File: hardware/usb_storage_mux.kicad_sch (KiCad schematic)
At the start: 24 parts, among them J7 USB3_B, J8 USB3_B_Micro, J9 USB3_A, U6 TMUXHS4212

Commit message: WIP 1.1
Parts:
- removed J7: USB3_B, USB3Wurth:Wurth WR-COM USB 3.0 692221030100, symbol Connector:USB3_B
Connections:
- net HOST_DN renamed SHOST_DN
- net HOST_DP renamed SHOST_DP
- net HOST_SSRXN renamed SHOST_SSRXN
- net HOST_SSRXP renamed SHOST_SSRXP
- net HOST_SSTXN renamed SHOST_SSTXN
- net HOST_SSTXP renamed SHOST_SSTXP
- net _HOST_SSRXN renamed _SHOST_SSRXN
- net _HOST_SSRXP renamed _SHOST_SSRXP

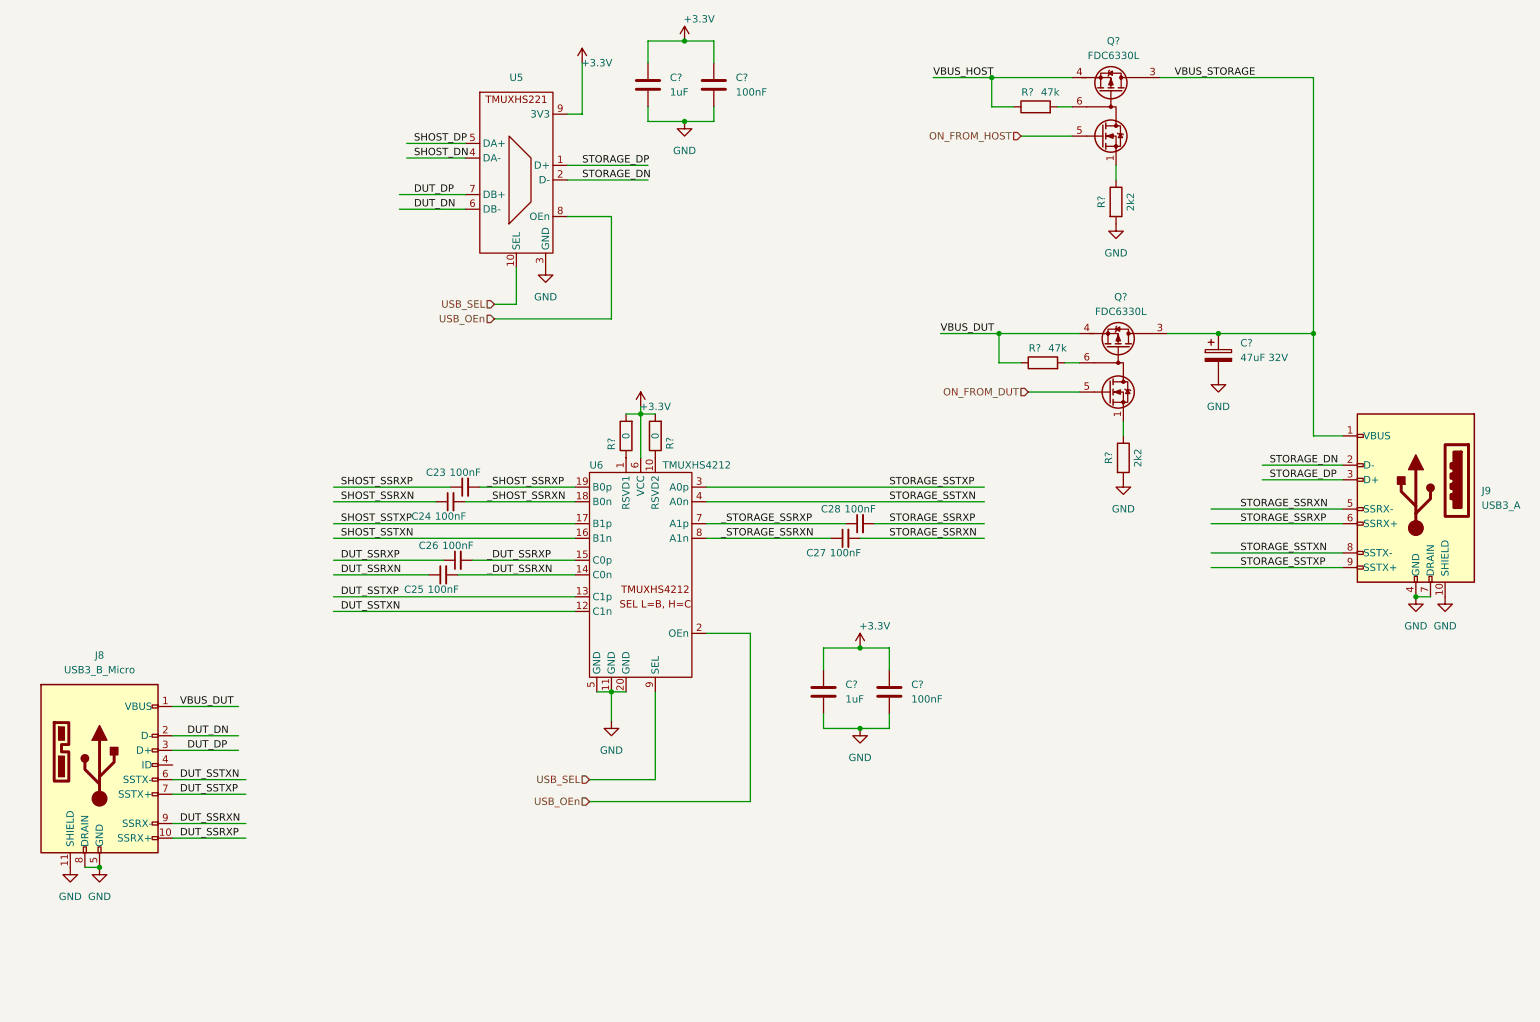
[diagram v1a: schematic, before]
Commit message: Started routing USB3 diff pairs
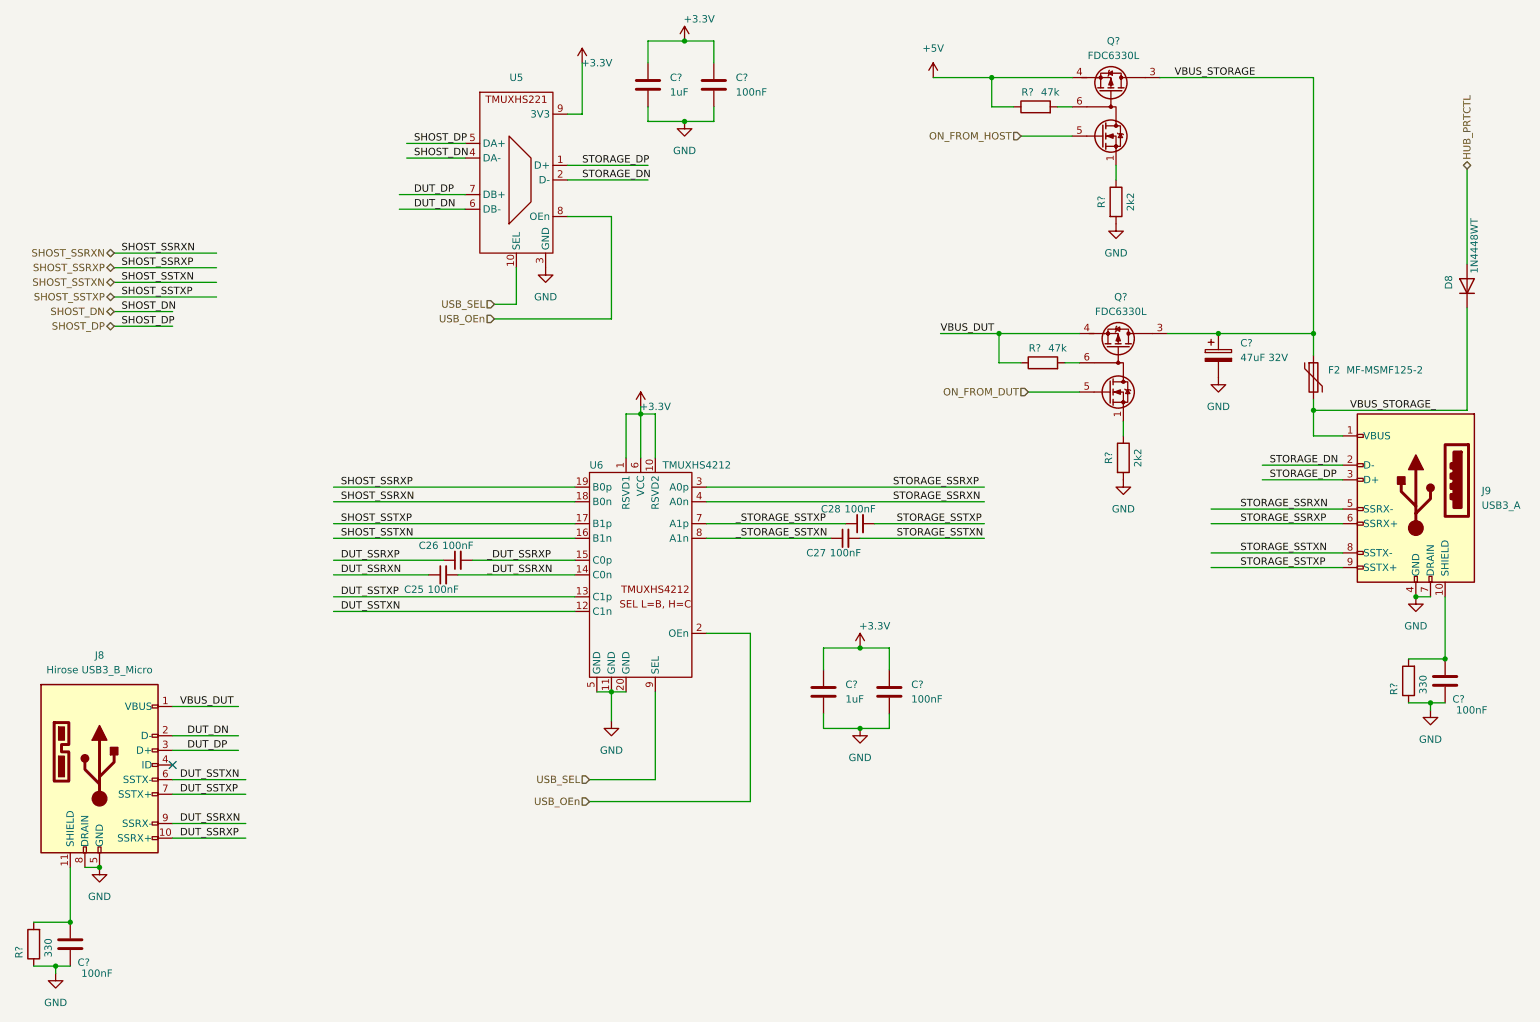
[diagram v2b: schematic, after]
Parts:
- removed C23, C24: 100nF, Capacitor_SMD:C_0402_1005Metric, symbol Device:C_Small
- removed R? (x2): 0, Resistor_SMD:R_0603_1608Metric, symbol Device:R
- added C? (x2): 100nF, Capacitor_SMD:C_0402_1005Metric, symbol Device:C
- added D8: 1N4448WT, Diode_SMD:D_SOD-523, symbol Diode:1N4448WT
- added F2: MF-MSMF125-2, FOOTPRINTS:MF-MSMF125-2, symbol Device:Polyfuse
- added R? (x2): 330, Resistor_SMD:R_0402_1005Metric, symbol Device:R
- C25, C26, C27, C28, C? (x2): MPN (none) -> CL05B104K05NNNC; MPN2 (none) -> TCC0402X7R104M160AT
- J8: value USB3_B_Micro -> Hirose USB3_B_Micro; footprint Connector_USB:USB3_Micro-B_Connfly_DS1104-01 -> FOOTPRINTS:ZX360DB10P30; Link (none) -> https://www.mouser.es/c/connectors/usb-connectors/?product=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; MPN (none) -> ZX360D-B-10P(30)
- R? (x4): footprint Resistor_SMD:R_0603_1608Metric -> Resistor_SMD:R_0402_1005Metric
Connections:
- net _SHOST_SSRXN is gone; now on net SHOST_SSRXN: U6.18 (B0n)
- net _SHOST_SSRXP is gone; now on net SHOST_SSRXP: U6.19 (B0p)
- net +3.3V: now also U6.1 (RSVD1), U6.10 (RSVD2)
- net GND: now also C?.2, C?.2, R?.1, R?.1; no longer J8.11 (SHIELD), J9.10 (SHIELD)
- net STORAGE_SSRXN: now also U6.4 (A0n); no longer C27.2
- net STORAGE_SSRXP: now also U6.3 (A0p); no longer C28.2
- net STORAGE_SSTXN: now also C27.2; no longer U6.4 (A0n)
- net STORAGE_SSTXP: now also C28.2; no longer U6.3 (A0p)
- net VBUS_STORAGE: now also F2.1; no longer J9.1 (VBUS)
- net VBUS_HOST renamed +5V
- net _STORAGE_SSRXN renamed _STORAGE_SSTXN
- net _STORAGE_SSRXP renamed _STORAGE_SSTXP
- new net: C?.1, J8.11 (SHIELD), R?.2
- new net: C?.1, J9.10 (SHIELD), R?.2
- new net HUB_PRTCTL: D8.2 (A)
- new net VBUS_STORAGE_: D8.1 (K), F2.2, J9.1 (VBUS)
- no-connect marks 0 -> 1

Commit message: Routing and several design fixes
Signed-off-by: Miguel Angel Ajo Pelayo <majopela@redhat.com>
Signed-off-by: Ricardo Noriega <rnoriega@redhat.com>
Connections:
- net GND: now also U6.21 (GND)
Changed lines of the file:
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@@
+    (stroke (width 0) (type default))
+  )
+  (wire (pts (xy 133.35 142.24) (xy 133.35 147.32))
     (stroke (width 0) (type default))
   )
@@
     (pin "8")
     (pin "9")
+    (pin "21")
     (instances
       (project "jumpstarter"
@@
         )
       )
+    )
+  )
+  (symbol (lib_id "power:GND") (at 133.35 147.32 0) (unit 1)
+    (in_bom yes) (on_board yes) (dnp no) (fields_autoplaced)
+    (property "Reference" "#PWR047" (at 133.35 153.67 0)
+      (effects (font (size 1.27 1.27)) hide)
+    )
+    (property "Value" "GND" (at 133.35 152.4 0)
+      (effects (font (size 1.27 1.27)))
+    )
+    (property "Footprint" "" (at 133.35 147.32 0)
+      (effects (font (size 1.27 1.27)) hide)
+    )
+    (property "Datasheet" "" (at 133.35 147.32 0)
+      (effects (font (size 1.27 1.27)) hide)
+    )
+    (pin "1")
+    (instances
+      (project "jumpstarter"
+        (path "/5e49fb74-0a9b-4946-8b59-2b8244d10fd9/90c9b6c3-4525-4edf-8d73-ac39bc46dfd1"
+          (reference "#PWR047") (unit 1)
+        )
+      )

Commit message: Almost ready 2.0.0
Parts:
- C25, C26, C27, C28, C? (x4): MFN (none) -> CL10B104KB8NNNC
- C? (x2): footprint Capacitor_SMD:C_0402_1005Metric -> Capacitor_SMD:C_0603_1608Metric; MFN (none) -> CL10B105KA8NNNC; MPN (none) -> CL10B105KA8NNNC
- C?: MFN (none) -> HV470M035E055ETR; MPN (none) -> HV470M035E055ETR
- D8: Link (none) -> https://www2.mouser.com/ProductDetail/onsemi-Fairchild/1N44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; MFN (none) -> 1N4448WT; MPN (none) -> 1N4448WT
- F2: MFN (none) -> MF-MSMF125-2; MPN (none) -> MF-MSMF125-2
- J8: Link https://www.mouser.es/c/connectors/usb-connectors/?product=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 -> https://www2.mouser.com/ProductDetail/Hirose-Connector/ZX36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; MFN (none) -> ZX360D-B-10P(30)
- J9: Link (none) -> https://eu.mouser.com/ProductDetail/Molex/48393-0001?qs=4Ef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; MFN (none) -> 48393-0001; MPN (none) -> 48393-0001
- Q? (x2): Link (none) -> https://www.mouser.es/ProductDetail/onsemi-Fairchild/FDC633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; MFN (none) -> FDC6330L; MPN (none) -> FDC6330L
- R? (x2): MFN (none) -> RTT024702FTH; MPN (none) -> RTT024702FTH
- R? (x2): MFN (none) -> RTT022201FTH; MPN (none) -> RTT022201FTH
- R? (x2): MFN (none) -> RTT02331JTH; MPN (none) -> RTT02331JTH
- U5: value ~ -> TMUXHS221; Link (none) -> https://eu.mouser.com/ProductDetail/Texas-Instruments/TMUXH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; MFN (none) -> TMUXHS221NKGR; MPN (none) -> TMUXHS221NKGR
- U6: Link (none) -> https://eu.mouser.com/ProductDetail/Texas-Instruments/TMUXH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; MFN (none) -> TMUXHS4212RKSR; MPN (none) -> TMUXHS4212RKSR
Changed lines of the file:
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@@
+      (effects (font (size 1.27 1.27)) hide)
+    )
+    (property "MFN" "RTT024702FTH" (at 195.58 85.09 0)
+      (effects (font (size 1.27 1.27)) hide)
+    )
+    (property "MPN" "RTT024702FTH" (at 195.58 85.09 0)
       (effects (font (size 1.27 1.27)) hide)
     )
@@
       (effects (font (size 1.27 1.27)) hide)
     )
+    (property "MFN" "CL10B104KB8NNNC" (at 163.83 113.03 0)
+      (effects (font (size 1.27 1.27)) hide)
+    )
     (pin "1")
     (pin "2")
@@
     )
     (property "Datasheet" "https://www.onsemi.com/pub/Collateral/FDC6330L-D.PDF" (at 207.01 90.17 0)
+      (effects (font (size 1.27 1.27)) hide)
+    )
+    (property "Link" "https://www.mouser.es/ProductDetail/onsemi-Fairchild/FDC6330L?qs=efMQ9B2bthfkfJJoj5%252B07g%3D%3D" (at 209.55 87.63 0)
+      (effects (font (size 1.27 1.27)) hide)
+    )
+    (property "MFN" "FDC6330L" (at 209.55 87.63 0)
+      (effects (font (size 1.27 1.27)) hide)
+    )
+    (property "MPN" "FDC6330L" (at 209.55 87.63 0)
       (effects (font (size 1.27 1.27)) hide)
     )
@@
       (effects (font (size 1.27 1.27)) hide)
     )
-    (property "Link" "https://www.mouser.es/c/connectors/usb-connectors/?product=Micro%20USB%20Type%20B%20Connectors&standard=USB%203.0&termination%20style=SMD%2FSMT&instock=y" (at 31.75 154.94 0)
+    (property "Link" "https://www2.mouser.com/ProductDetail/Hirose-Connector/ZX360D-B-10P30?qs=4J5DPWWS9EDezzYtx6NKEg%3D%3D" (at 31.75 154.94 0)
+      (effects (font (size 1.27 1.27)) hide)
+    )
+    (property "MFN" "ZX360D-B-10P(30)" (at 31.75 154.94 0)
       (effects (font (size 1.27 1.27)) hide)
     )
@@
       (effects (font (size 1.27 1.27)) hide)
     )
+    (property "MFN" "CL10B104KB8NNNC" (at 26.67 186.055 0)
+      (effects (font (size 1.27 1.27)) hide)
+    )
     (pin "1")
     (pin "2")
@@
       (effects (font (size 1.27 1.27)) (justify left))
     )
-    (property "Footprint" "Capacitor_SMD:C_0402_1005Metric" (at 158.4452 146.05 0)
+    (property "Footprint" "Capacitor_SMD:C_0603_1608Metric" (at 158.4452 146.05 0)
       (effects (font (size 1.27 1.27)) hide)
     )
@@
       (effects (font (size 1.27 1.27)) hide)
     )
+    (property "MFN" "CL10B105KA8NNNC" (at 157.48 142.24 0)
+      (effects (font (size 1.27 1.27)) hide)
+    )
+    (property "MPN" "CL10B105KA8NNNC" (at 157.48 142.24 0)
+      (effects (font (size 1.27 1.27)) hide)
+    )
     (pin "1")
     (pin "2")
@@
       (effects (font (size 1.27 1.27)) hide)
     )
+    (property "MFN" "RTT024702FTH" (at 194.31 40.64 0)
+      (effects (font (size 1.27 1.27)) hide)
+    )
+    (property "MPN" "RTT024702FTH" (at 194.31 40.64 0)
+      (effects (font (size 1.27 1.27)) hide)
+    )
     (pin "1")
     (pin "2")
@@
       (effects (font (size 1.27 1.27)) hide)
     )
+    (property "MFN" "RTT022201FTH" (at 208.28 57.15 0)
+      (effects (font (size 1.27 1.27)) hide)
+    )
+    (property "MPN" "RTT022201FTH" (at 208.28 57.15 0)
+      (effects (font (size 1.27 1.27)) hide)
+    )
     (pin "1")
     (pin "2")
@@
       (effects (font (size 1.27 1.27)) hide)
     )
+    (property "MFN" "CL10B104KB8NNNC" (at 91.44 121.92 0)
+      (effects (font (size 1.27 1.27)) hide)
+    )
     (pin "1")
     (pin "2")
@@
     )
     (property "Sim.Pins" "1=K 2=A" (at 269.24 71.755 0)
+      (effects (font (size 1.27 1.27)) hide)
+    )
+    (property "Link" "https://www2.mouser.com/ProductDetail/onsemi-Fairchild/1N4448WT?qs=2%2FYqgE%252BHg%252BJEFyXf7B7EGw%3D%3D" (at 269.24 71.755 0)
+      (effects (font (size 1.27 1.27)) hide)
+    )
+    (property "MFN" "1N4448WT" (at 269.24 71.755 0)
+      (effects (font (size 1.27 1.27)) hide)
+    )
+    (property "MPN" "1N4448WT" (at 269.24 71.755 0)
       (effects (font (size 1.27 1.27)) hide)
     )
@@
       (effects (font (size 1.27 1.27)) hide)
     )
+    (property "MFN" "CL10B104KB8NNNC" (at 168.91 142.24 0)
+      (effects (font (size 1.27 1.27)) hide)
+    )
     (pin "1")
     (pin "2")
@@
     )
     (property "Datasheet" "~" (at 259.08 140.335 0)
+      (effects (font (size 1.27 1.27)) hide)
+    )
+    (property "MFN" "RTT02331JTH" (at 259.08 140.335 0)
+      (effects (font (size 1.27 1.27)) hide)
+    )
+    (property "MPN" "RTT02331JTH" (at 259.08 140.335 0)
       (effects (font (size 1.27 1.27)) hide)
     )
@@
     )
     (property "Datasheet" "~" (at 256.54 105.41 0)
+      (effects (font (size 1.27 1.27)) hide)
+    )
+    (property "Link" "https://eu.mouser.com/ProductDetail/Molex/48393-0001?qs=4Ef8CTzXwRfUk7%252BJCOVflQ%3D%3D&_gl=1*l7r4pu*_ga*dW5kZWZpbmVk*_ga_15W4STQT4T*MTcwMjM3NTI2MC40MC4xLjE3MDIzNzUyNjEuNTkuMC4w" (at 260.35 107.95 0)
+      (effects (font (size 1.27 1.27)) hide)
+    )
+    (property "MFN" "48393-0001" (at 260.35 107.95 0)
+      (effects (font (size 1.27 1.27)) hide)
+    )
+    (property "MPN" "48393-0001" (at 260.35 107.95 0)
       (effects (font (size 1.27 1.27)) hide)
     )
@@
       (effects (font (size 1.27 1.27)) hide)
     )
+    (property "Description" "6V 1.25 A Resetable fuse" (at 242.57 87.63 0)
+      (effects (font (size 1.27 1.27)) hide)
+    )
+    (property "MFN" "MF-MSMF125-2" (at 242.57 87.63 0)
+      (effects (font (size 1.27 1.27)) hide)
+    )
+    (property "MPN" "MF-MSMF125-2" (at 242.57 87.63 0)
+      (effects (font (size 1.27 1.27)) hide)
+    )
     (pin "1")
     (pin "2")
@@
     )
     (property "Datasheet" "https://www.onsemi.com/pub/Collateral/FDC6330L-D.PDF" (at 205.74 45.72 0)
+      (effects (font (size 1.27 1.27)) hide)
+    )
+    (property "Link" "https://www.mouser.es/ProductDetail/onsemi-Fairchild/FDC6330L?qs=efMQ9B2bthfkfJJoj5%252B07g%3D%3D" (at 208.28 43.18 0)
+      (effects (font (size 1.27 1.27)) hide)
+    )
+    (property "MFN" "FDC6330L" (at 208.28 43.18 0)
+      (effects (font (size 1.27 1.27)) hide)
+    )
+    (property "MPN" "FDC6330L" (at 208.28 43.18 0)
       (effects (font (size 1.27 1.27)) hide)
     )
@@
       (effects (font (size 1.27 1.27)) hide)
     )
+    (property "MFN" "RTT02331JTH" (at 20.32 186.055 0)
+      (effects (font (size 1.27 1.27)) hide)
+    )
+    (property "MPN" "RTT02331JTH" (at 20.32 186.055 0)
+      (effects (font (size 1.27 1.27)) hide)
+    )
     (pin "1")
     (pin "2")
@@
       (effects (font (size 1.27 1.27)) (justify left))
     )
-    (property "Footprint" "Capacitor_SMD:C_0402_1005Metric" (at 127.9652 40.64 0)
+    (property "Footprint" "Capacitor_SMD:C_0603_1608Metric" (at 127.9652 40.64 0)
       (effects (font (size 1.27 1.27)) hide)
     )
@@
       (effects (font (size 1.27 1.27)) hide)
     )
+    (property "MFN" "CL10B105KA8NNNC" (at 127 36.83 0)
+      (effects (font (size 1.27 1.27)) hide)
+    )
+    (property "MPN" "CL10B105KA8NNNC" (at 127 36.83 0)
+      (effects (font (size 1.27 1.27)) hide)
+    )
     (pin "1")
     (pin "2")
@@
     )
     (property "MPN2" "TCC0402X7R104M160AT" (at 93.98 119.38 0)
+      (effects (font (size 1.27 1.27)) hide)
+    )
+    (property "MFN" "CL10B104KB8NNNC" (at 93.98 119.38 0)
       (effects (font (size 1.27 1.27)) hide)
     )
@@
     )
     (property "Datasheet" "https://www.ti.com/lit/ds/symlink/tmuxhs4212.pdf" (at 119.38 102.87 0)
+      (effects (font (size 1.27 1.27)) hide)
+    )
+    (property "Link" "https://eu.mouser.com/ProductDetail/Texas-Instruments/TMUXHS4212RKSR?qs=7MVldsJ5UawhO1PzGdCV7Q%3D%3" (at 119.38 102.87 0)
+      (effects (font (size 1.27 1.27)) hide)
+    )
+    (property "MFN" "TMUXHS4212RKSR" (at 119.38 102.87 0)
+      (effects (font (size 1.27 1.27)) hide)
+    )
+    (property "MPN" "TMUXHS4212RKSR" (at 119.38 102.87 0)
       (effects (font (size 1.27 1.27)) hide)
     )
@@
       (effects (font (size 1.27 1.27)) hide)
     )
+    (property "MFN" "CL10B104KB8NNNC" (at 161.29 115.57 0)
+      (effects (font (size 1.27 1.27)) hide)
+    )
     (pin "1")
     (pin "2")
@@
       (effects (font (size 1.27 1.27)) hide)
     )
+    (property "MFN" "CL10B104KB8NNNC" (at 138.43 36.83 0)
+      (effects (font (size 1.27 1.27)) hide)
+    )
     (pin "1")
     (pin "2")
@@
       (effects (font (size 1.27 1.27)) hide)
     )
+    (property "Description" "47uF 32V 6.3x5.4 SMD Electrolytic Capacitor" (at 226.06 83.82 0)
+      (effects (font (size 1.27 1.27)) hide)
+    )
+    (property "MFN" "HV470M035E055ETR" (at 226.06 83.82 0)
+      (effects (font (size 1.27 1.27)) hide)
+    )
+    (property "MPN" "HV470M035E055ETR" (at 226.06 83.82 0)
+      (effects (font (size 1.27 1.27)) hide)
+    )
     (pin "1")
     (pin "2")
@@
       (effects (font (size 1.27 1.27)))
     )
-    (property "Value" "~" (at 96.52 46.99 0)
+    (property "Value" "TMUXHS221" (at 96.52 46.99 0)
       (effects (font (size 1.27 1.27)))
     )
@@
     )
     (property "Datasheet" "https://www.ti.com/product/TMUXHS221" (at 96.52 46.99 0)
+      (effects (font (size 1.27 1.27)) hide)
+    )
+    (property "Link" "https://eu.mouser.com/ProductDetail/Texas-Instruments/TMUXHS221NKGR?qs=IPgv5n7u5QbuI%2Forjo3H9g%3D%3D" (at 96.52 46.99 0)
+      (effects (font (size 1.27 1.27)) hide)
+    )
+    (property "MFN" "TMUXHS221NKGR" (at 96.52 46.99 0)
+      (effects (font (size 1.27 1.27)) hide)
+    )
+    (property "MPN" "TMUXHS221NKGR" (at 96.52 46.99 0)
       (effects (font (size 1.27 1.27)) hide)
     )
@@
       (effects (font (size 1.27 1.27)) hide)
     )
+    (property "MFN" "RTT022201FTH" (at 209.55 101.6 0)
+      (effects (font (size 1.27 1.27)) hide)
+    )
+    (property "MPN" "RTT022201FTH" (at 209.55 101.6 0)
+      (effects (font (size 1.27 1.27)) hide)
+    )
     (pin "1")
     (pin "2")
@@
       (effects (font (size 1.27 1.27)) hide)
     )
+    (property "MFN" "CL10B104KB8NNNC" (at 265.43 140.335 0)
+      (effects (font (size 1.27 1.27)) hide)
+    )
